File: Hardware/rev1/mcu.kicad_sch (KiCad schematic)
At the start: 9 parts, among them U0 STM32F103C8Tx, Y1 16MHz

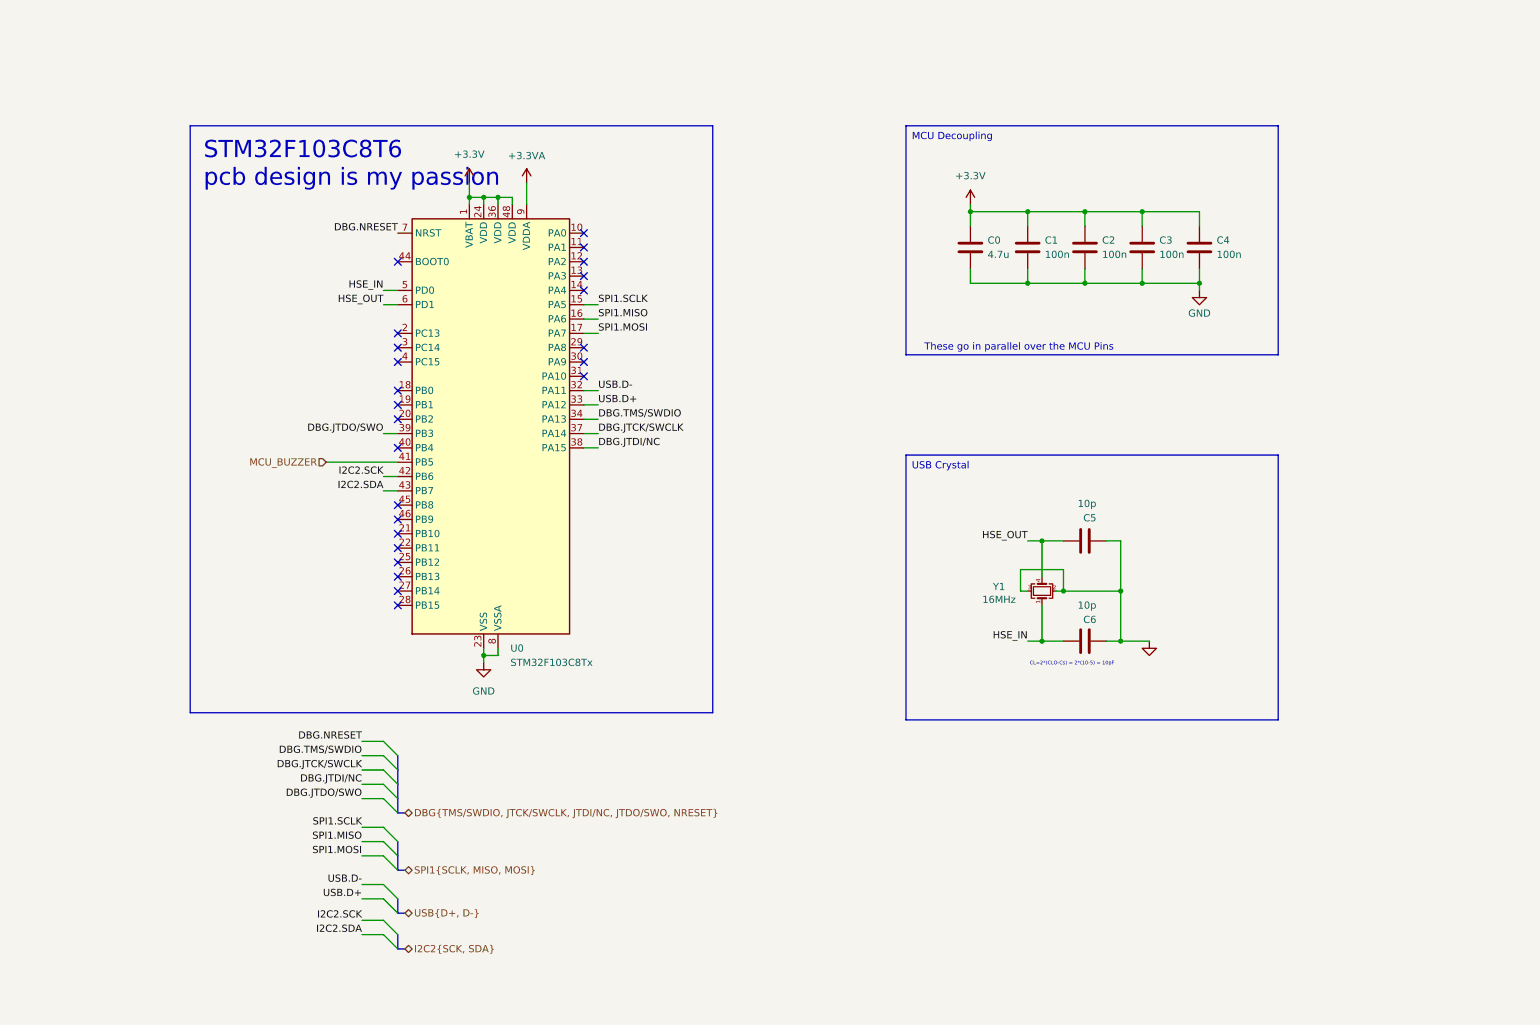
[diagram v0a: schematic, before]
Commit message: GitHub Shenanegans - Taken things from Shon's commit because easier to fix that way than to figure out how to merge properly
Literally for the buzzer and switch, hopefully retain the capacitor fix
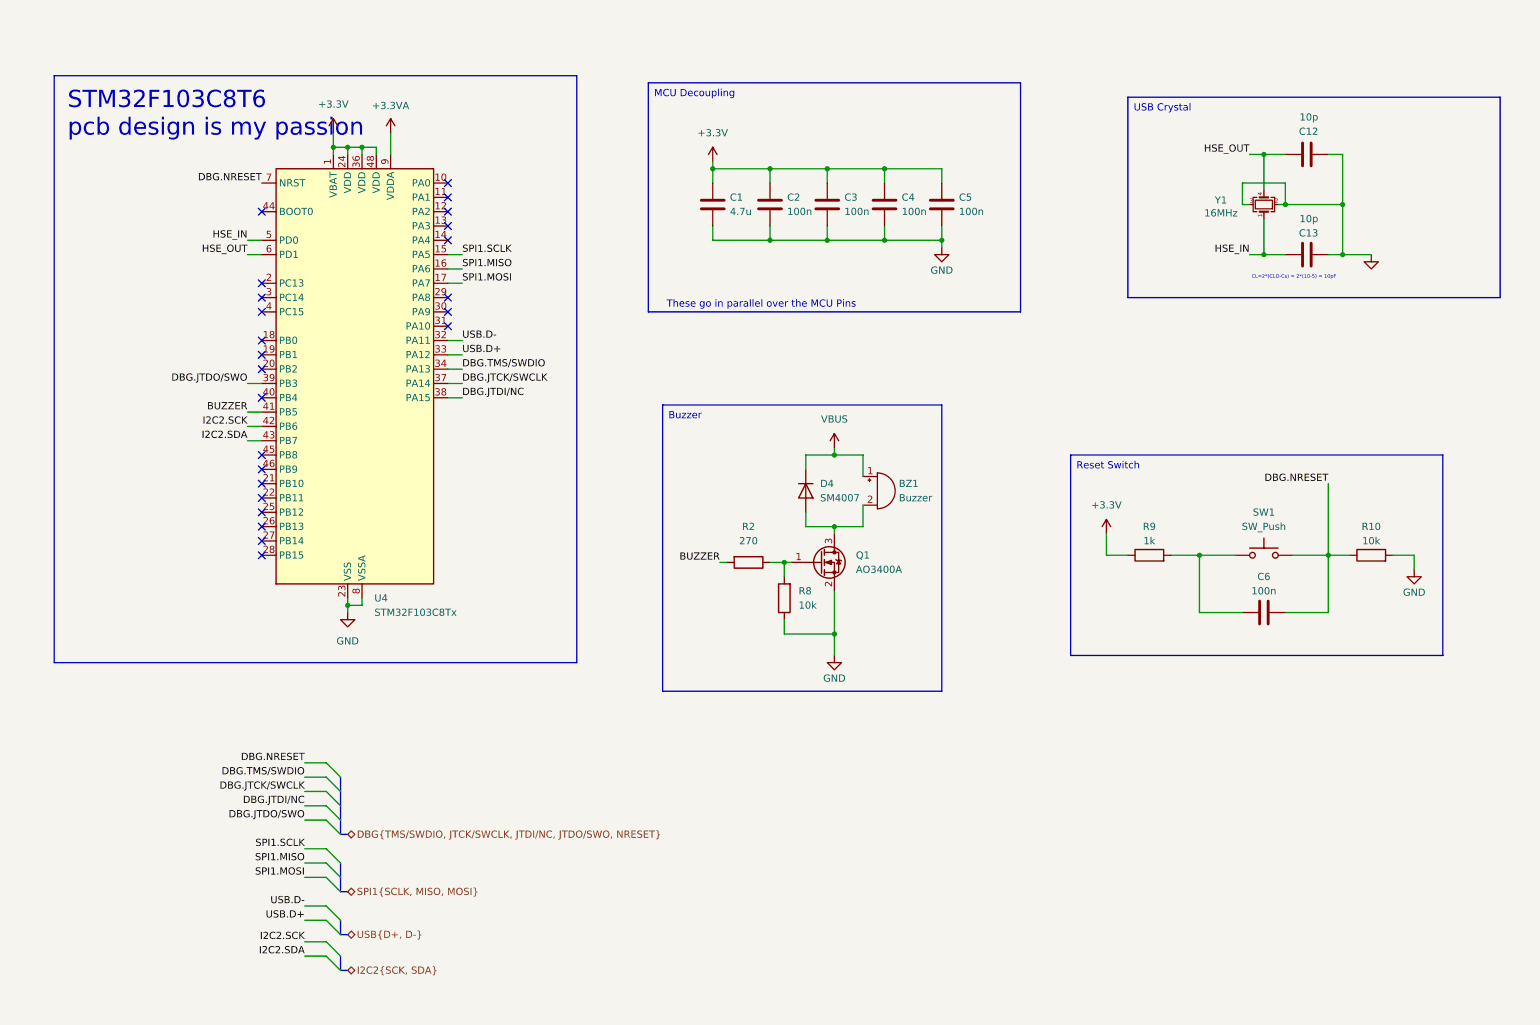
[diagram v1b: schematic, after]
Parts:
- removed C0: 4.7u, symbol Device:C
- removed U0: STM32F103C8Tx, Package_QFP:LQFP-48_7x7mm_P0.5mm, symbol MCU_ST_STM32F1:STM32F103C8Tx
- added BZ1: Buzzer, Buzzer_Beeper:MagneticBuzzer_Kingstate_KCG0601, symbol Device:Buzzer
- added C12, C13: 10p, Capacitor_SMD:C_0402_1005Metric, symbol Device:C
- added D4: SM4007, Diode_SMD:D_SOD-123F, symbol Diode:SM4007
- added Q1: AO3400A, Package_TO_SOT_SMD:SOT-23, symbol Transistor_FET:AO3400A
- added R10, R8: 10k, Resistor_SMD:R_0603_1608Metric, symbol Device:R
- added R2: 270, Resistor_SMD:R_0603_1608Metric, symbol Device:R
- added R9: 1k, Resistor_SMD:R_0603_1608Metric, symbol Device:R
- added SW1: SW_Push, Button_Switch_SMD:SW_Push_1P1T_XKB_TS-1187A, symbol Switch:SW_Push
- added U4: STM32F103C8Tx, Package_QFP:LQFP-48_7x7mm_P0.5mm, symbol MCU_ST_STM32F1:STM32F103C8Tx
- C1: value 100n -> 4.7u; footprint (none) -> Buzzer_Beeper:MagneticBuzzer_Kingstate_KCG0601
- C2, C3, C4: footprint (none) -> Capacitor_SMD:C_0402_1005Metric
- C5, C6: value 10p -> 100n
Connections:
- net +3.3V: now also C5.1, R9.1, U4.1 (VBAT), U4.24 (VDD), U4.36 (VDD), U4.48 (VDD)
- net +3.3VA: now also U4.9 (VDDA)
- net DBG.JTCK/SWCLK: now also U4.37 (PA14)
- net DBG.JTDI/NC: now also U4.38 (PA15)
- net DBG.JTDO/SWO: now also U4.39 (PB3)
- net DBG.NRESET: now also C6.2, R10.1, SW1.2, U4.7 (NRST)
- net DBG.TMS/SWDIO: now also U4.34 (PA13)
- net GND: now also C12.2, C13.2, Q1.2 (S), R10.2, R8.1, U4.23 (VSS), U4.35 (VSS), U4.47 (VSS), U4.8 (VSSA); no longer C6.2
- net HSE_IN: now also C13.1, U4.5 (PD0); no longer C6.1
- net HSE_OUT: now also C12.1, U4.6 (PD1); no longer C5.1
- net I2C2.SCK: now also U4.42 (PB6)
- net I2C2.SDA: now also U4.43 (PB7)
- net SPI1.MISO: now also U4.16 (PA6)
- net SPI1.MOSI: now also U4.17 (PA7)
- net SPI1.SCLK: now also U4.15 (PA5)
- net USB.D+: now also U4.33 (PA12)
- net USB.D-: now also U4.32 (PA11)
- new net: Q1.1 (G), R2.1, R8.2
- new net: BZ1.2 (-), D4.2 (A), Q1.3 (D)
- new net: C6.1, R9.2, SW1.1
- new net BUZZER: R2.2, U4.41 (PB5)
- new net VBUS: BZ1.1 (+), D4.1 (K)

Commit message: Literal Progress
PCB populated, schematic changed, all pins on MCU accessible from headers, all components on board, traces required
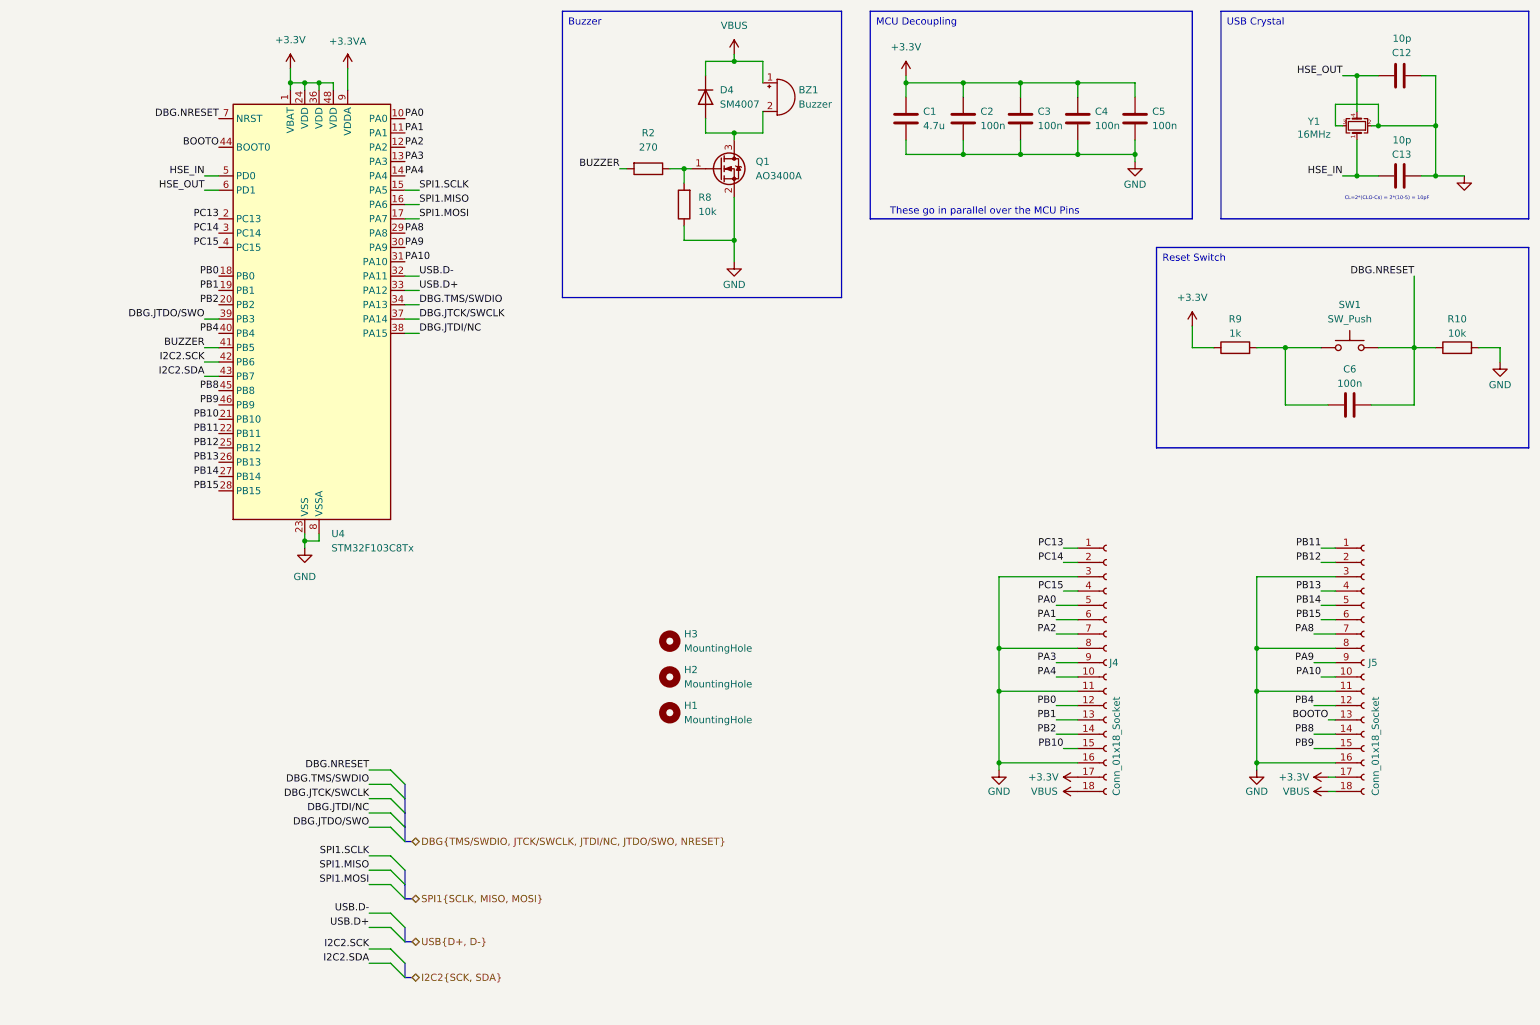
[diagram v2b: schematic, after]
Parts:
- added H1, H2, H3: MountingHole, MountingHole:MountingHole_3.2mm_M3, symbol Mechanical:MountingHole
- added J4, J5: Conn_01x18_Socket, Connector_PinHeader_1.00mm:PinHeader_1x18_P1.00mm_Vertical, symbol Connector:Conn_01x18_Socket
- C1: footprint Buzzer_Beeper:MagneticBuzzer_Kingstate_KCG0601 -> Capacitor_SMD:C_0603_1608Metric
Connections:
- net +3.3V: now also J4.17 (Pin_17), J5.17 (Pin_17)
- net GND: now also J4.11 (Pin_11), J4.16 (Pin_16), J4.3 (Pin_3), J4.8 (Pin_8), J5.11 (Pin_11), J5.16 (Pin_16), J5.3 (Pin_3), J5.8 (Pin_8)
- net VBUS: now also J4.18 (Pin_18), J5.18 (Pin_18)
- net PA0: now reaches U4.10 (PA0)
- net PA0: now also J4.5 (Pin_5)
- net PA1: now reaches U4.11 (PA1)
- net PA1: now also J4.6 (Pin_6)
- net PA2: now reaches U4.12 (PA2)
- net PA2: now also J4.7 (Pin_7)
- net PA3: now reaches U4.13 (PA3)
- net PA3: now also J4.9 (Pin_9)
- net PA4: now reaches U4.14 (PA4)
- net PA4: now also J4.10 (Pin_10)
- net PB0: now reaches U4.18 (PB0)
- net PB0: now also J4.12 (Pin_12)
- net PB1: now reaches U4.19 (PB1)
- net PB1: now also J4.13 (Pin_13)
- net PC13: now reaches U4.2 (PC13)
- net PC13: now also J4.1 (Pin_1)
- net PB2: now reaches U4.20 (PB2)
- net PB2: now also J4.14 (Pin_14)
- net PB10: now reaches U4.21 (PB10)
- net PB10: now also J4.15 (Pin_15)
- net PB11: now reaches U4.22 (PB11)
- net PB11: now also J5.1 (Pin_1)
- net PB12: now reaches U4.25 (PB12)
- net PB12: now also J5.2 (Pin_2)
- net PB13: now reaches U4.26 (PB13)
- net PB13: now also J5.4 (Pin_4)
- net PB14: now reaches U4.27 (PB14)
- net PB14: now also J5.5 (Pin_5)
- net PB15: now reaches U4.28 (PB15)
- net PB15: now also J5.6 (Pin_6)
- net PA8: now reaches U4.29 (PA8)
- net PA8: now also J5.7 (Pin_7)
- net PC14: now reaches U4.3 (PC14)
- net PC14: now also J4.2 (Pin_2)
- net PA9: now reaches U4.30 (PA9)
- net PA9: now also J5.9 (Pin_9)
- net PA10: now reaches U4.31 (PA10)
- net PA10: now also J5.10 (Pin_10)
- net PC15: now reaches U4.4 (PC15)
- net PC15: now also J4.4 (Pin_4)
- net PB4: now reaches U4.40 (PB4)
- net PB4: now also J5.12 (Pin_12)
- net BOOTO: now reaches U4.44 (BOOT0)
- net BOOTO: now also J5.13 (Pin_13)
- net PB8: now reaches U4.45 (PB8)
- net PB8: now also J5.14 (Pin_14)
- net PB9: now reaches U4.46 (PB9)
- net PB9: now also J5.15 (Pin_15)
- no-connect marks 24 -> 0
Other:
- moved on the sheet: BZ1, C1, C12, C13, C2, C3, C4, C5, C6, D4, Q1, R10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

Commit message: Defucked the header net assignments, cleaned up schematic sheet, routed to headers
routing is uninformed, took care to allow ground planes to not become islands however there are some sketchy looking bits. Power still requires routing and we are really tight on space so will likely either need to redo all those traces for priority for 3.3V or weave power in between them
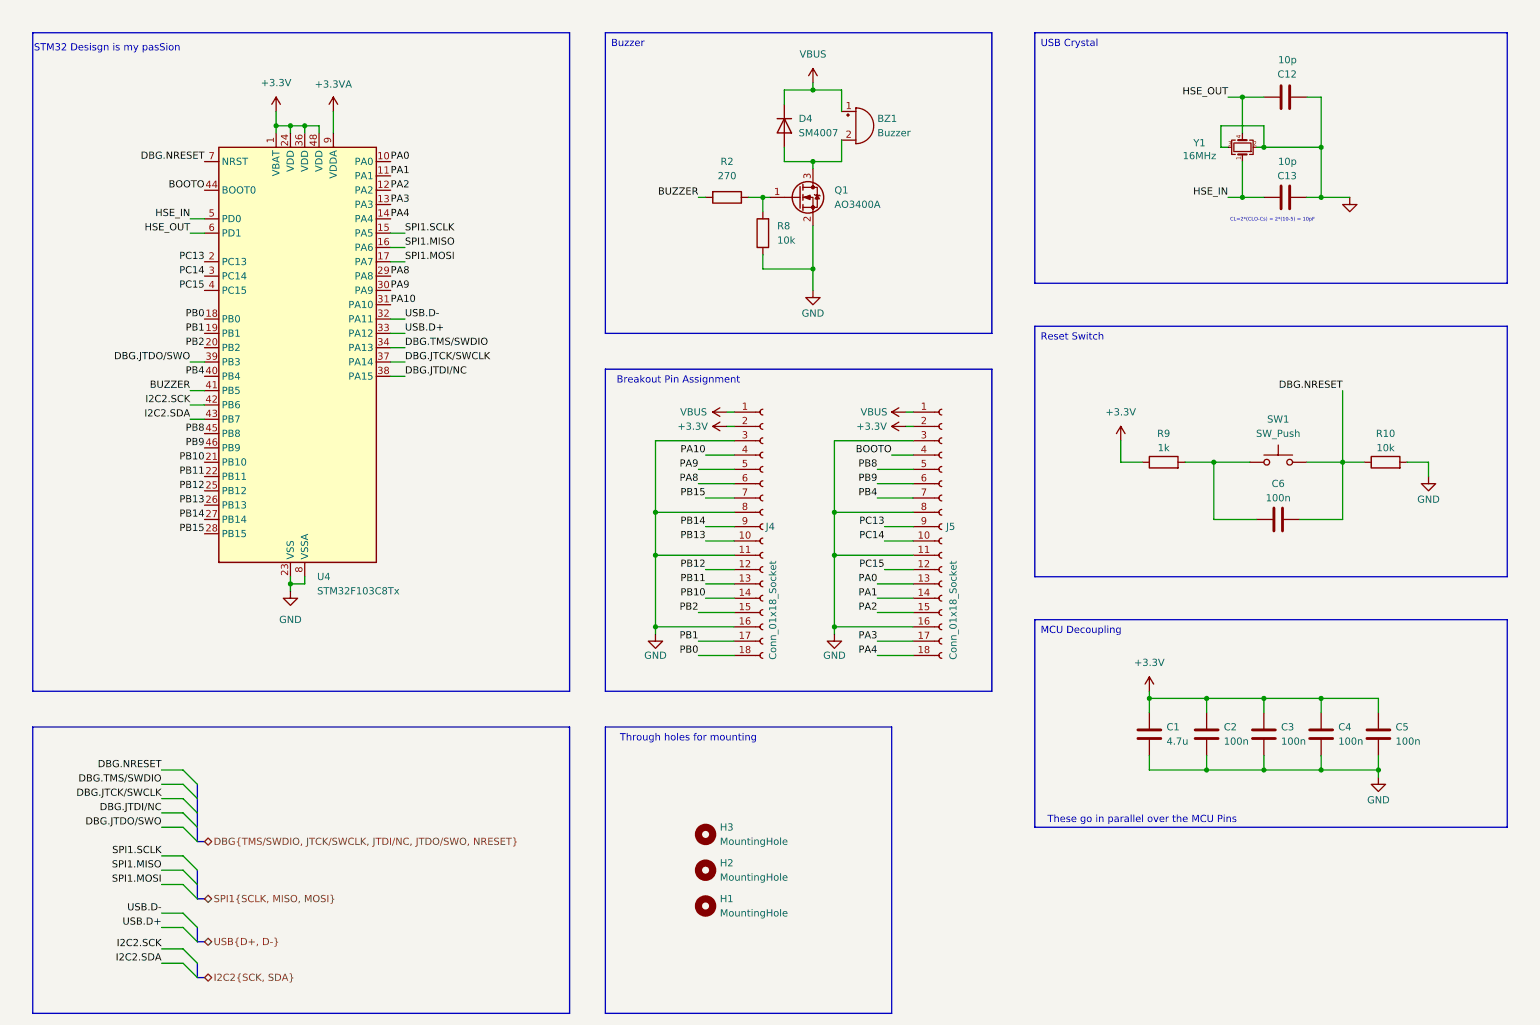
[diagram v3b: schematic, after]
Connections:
- net +3.3V: now also J4.2 (Pin_2), J5.2 (Pin_2); no longer J4.17 (Pin_17), J5.17 (Pin_17)
- net BOOTO: now also J5.4 (Pin_4); no longer J5.13 (Pin_13)
- net PA0: now also J5.13 (Pin_13); no longer J4.5 (Pin_5)
- net PA1: now also J5.14 (Pin_14); no longer J4.6 (Pin_6)
- net PA10: now also J4.4 (Pin_4); no longer J5.10 (Pin_10)
- net PA2: now also J5.15 (Pin_15); no longer J4.7 (Pin_7)
- net PA3: now also J5.17 (Pin_17); no longer J4.9 (Pin_9)
- net PA4: now also J5.18 (Pin_18); no longer J4.10 (Pin_10)
- net PA8: now also J4.6 (Pin_6); no longer J5.7 (Pin_7)
- net PA9: now also J4.5 (Pin_5); no longer J5.9 (Pin_9)
- net PB0: now also J4.18 (Pin_18); no longer J4.12 (Pin_12)
- net PB1: now also J4.17 (Pin_17); no longer J4.13 (Pin_13)
- net PB10: now also J4.14 (Pin_14); no longer J4.15 (Pin_15)
- net PB11: now also J4.13 (Pin_13); no longer J5.1 (Pin_1)
- net PB12: now also J4.12 (Pin_12); no longer J5.2 (Pin_2)
- net PB13: now also J4.10 (Pin_10); no longer J5.4 (Pin_4)
- net PB14: now also J4.9 (Pin_9); no longer J5.5 (Pin_5)
- net PB15: now also J4.7 (Pin_7); no longer J5.6 (Pin_6)
- net PB2: now also J4.15 (Pin_15); no longer J4.14 (Pin_14)
- net PB4: now also J5.7 (Pin_7); no longer J5.12 (Pin_12)
- net PB8: now also J5.5 (Pin_5); no longer J5.14 (Pin_14)
- net PB9: now also J5.6 (Pin_6); no longer J5.15 (Pin_15)
- net PC13: now also J5.9 (Pin_9); no longer J4.1 (Pin_1)
- net PC14: now also J5.10 (Pin_10); no longer J4.2 (Pin_2)
- net PC15: now also J5.12 (Pin_12); no longer J4.4 (Pin_4)
- net VBUS: now also J4.1 (Pin_1), J5.1 (Pin_1); no longer J4.18 (Pin_18), J5.18 (Pin_18)
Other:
- note added: "Breakout Pin Assignment"
- note added: "STM32 Desisgn is my pasSion"
- note added: "Through holes for mounting"
- moved on the sheet: BZ1, C1, C12, C13, C2, C3, C4, C5, C6, D4, H1, H2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

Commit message: No vallium for the whole week :(
Net tie footprint, moved breakouts, crystal we think is close enough, tried to look for debug interface but didn't find it. no vallies :(
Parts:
- removed H3: MountingHole, MountingHole:MountingHole_3.2mm_M3, symbol Mechanical:MountingHole
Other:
- moved on the sheet: H1, H2
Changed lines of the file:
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@@
 	(symbol
 		(lib_id "Mechanical:MountingHole")
-		(at 137.16 166.37 0)
+		(at 137.16 162.56 0)
 		(unit 1)
 		(exclude_from_sim yes)
@@
 		(fields_autoplaced yes)
 		(property "Reference" "H2"
-			(at 139.7 165.0999 0)
+			(at 139.7 161.2899 0)
 			(effects
 				(font
@@
 		)
 		(property "Value" "MountingHole"
-			(at 139.7 167.6399 0)
+			(at 139.7 163.8299 0)
 			(effects
 				(font
@@
 		)
 		(property "Footprint" "MountingHole:MountingHole_3.2mm_M3"
-			(at 137.16 166.37 0)
+			(at 137.16 162.56 0)
 			(effects
 				(font
@@
 		)
 		(property "Datasheet" "~"
-			(at 137.16 166.37 0)
+			(at 137.16 162.56 0)
 			(effects
 				(font
@@
 		)
 		(property "Description" "Mounting Hole without connection"
-			(at 137.16 166.37 0)
+			(at 137.16 162.56 0)
 			(effects
 				(font
@@
 	(symbol
 		(lib_id "Mechanical:MountingHole")
-		(at 137.16 172.72 0)
+		(at 137.16 168.91 0)
 		(unit 1)
 		(exclude_from_sim yes)
@@
 		(fields_autoplaced yes)
 		(property "Reference" "H1"
-			(at 139.7 171.4499 0)
+			(at 139.7 167.6399 0)
 			(effects
 				(font
@@
 		)
 		(property "Value" "MountingHole"
-			(at 139.7 173.9899 0)
+			(at 139.7 170.1799 0)
 			(effects
 				(font
@@
 		)
 		(property "Footprint" "MountingHole:MountingHole_3.2mm_M3"
-			(at 137.16 172.72 0)
+			(at 137.16 168.91 0)
 			(effects
 				(font
@@
 		)
 		(property "Datasheet" "~"
-			(at 137.16 172.72 0)
+			(at 137.16 168.91 0)
 			(effects
 				(font
@@
 		)
 		(property "Description" "Mounting Hole without connection"
-			(at 137.16 172.72 0)
+			(at 137.16 168.91 0)
 			(effects
 				(font
@@
 					(unit 1)
 				)
-			)
-		)
-	)
-	(symbol
-		(lib_id "Mechanical:MountingHole")
-		(at 137.16 160.02 0)
-		(unit 1)
-		(exclude_from_sim yes)
-		(in_bom no)
-		(on_board yes)
-		(dnp no)
-		(fields_autoplaced yes)
-		(property "Reference" "H3"
-			(at 139.7 158.7499 0)
-			(effects
-				(font
-					(size 1.27 1.27)
-				)
-				(justify left)
-			)
-		)
-		(property "Value" "MountingHole"
-			(at 139.7 161.2899 0)
-			(effects
-				(font
-					(size 1.27 1.27)
-				)
-				(justify left)
-			)
-		)
-		(property "Footprint" "MountingHole:MountingHole_3.2mm_M3"
-			(at 137.16 160.02 0)
-			(effects
-				(font
-					(size 1.27 1.27)
-				)
-				(hide yes)
-			)
-		)
-		(property "Datasheet" "~"
-			(at 137.16 160.02 0)
-			(effects
-				(font
-					(size 1.27 1.27)
-				)
-				(hide yes)
-			)
-		)
-		(property "Description" "Mounting Hole without connection"
-			(at 137.16 160.02 0)
-			(effects
-				(font
-					(size 1.27 1.27)
-				)
-				(hide yes)
-			)
-		)
-		(instances
-			(project "rev1"
-				(path "/e52639ab-1647-4d34-8bc5-5aadc4708147/1e23a58f-6de3-4599-8764-fd8b445df38e"
-					(reference "H3")
-					(unit 1)
-				)
